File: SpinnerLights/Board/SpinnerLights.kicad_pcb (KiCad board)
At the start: 2 copper layers, 78 x 74.1 mm, 14 parts, among them U1 SeeeduinoXIAO, U2 ADXL343

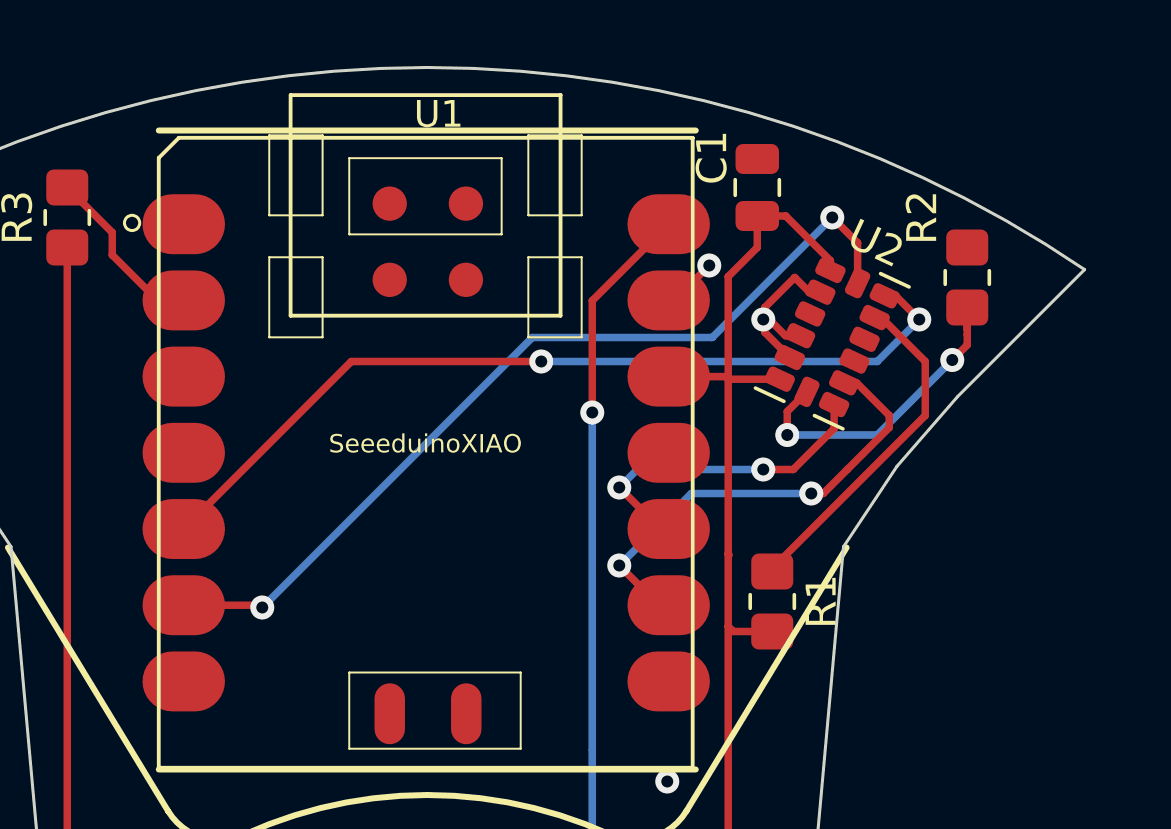
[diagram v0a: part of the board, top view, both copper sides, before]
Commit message: SpinnerLights: Fix I2C interface pins
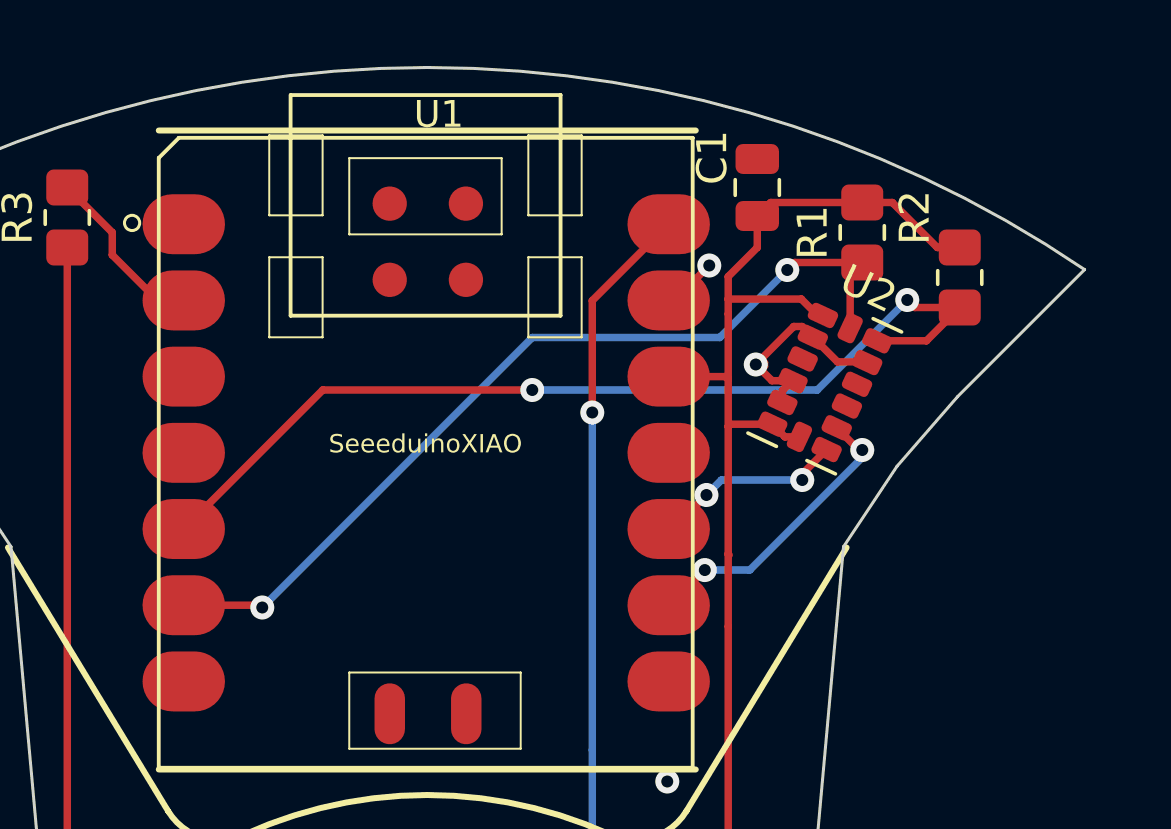
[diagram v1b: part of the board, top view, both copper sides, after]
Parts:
- moved R1 12.7 mm to (114.5, 66.5), turned to 90 degrees
- moved U2 1.52 mm to (113.2, 71.5)
- moved R2 0.25 mm to (117.8, 68.0)
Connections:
- R1 pad 1: Net-(R1-Pad1) -> SCL
- R2 pad 1: Net-(R2-Pad1) -> SDA
- R2 pad 2: GND -> +3V3
- U2 pad 12: Net-(R1-Pad1) -> GND
- U2 pad 7: Net-(R2-Pad1) -> +3V3
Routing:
- net Net-(R1-Pad1): track 11.4 -> 0.00 mm
- net Net-(R2-Pad1): track 11.0 -> 0.00 mm, vias 2 -> 0
- net +3V3: track 103.0 -> 110.1 mm
- net INT2: track 15.5 -> 10.2 mm
- net INT1: track 11.0 -> 6.74 mm
- net SDA: track 28.9 -> 32.3 mm
- net GND: track 13.3 -> 14.5 mm

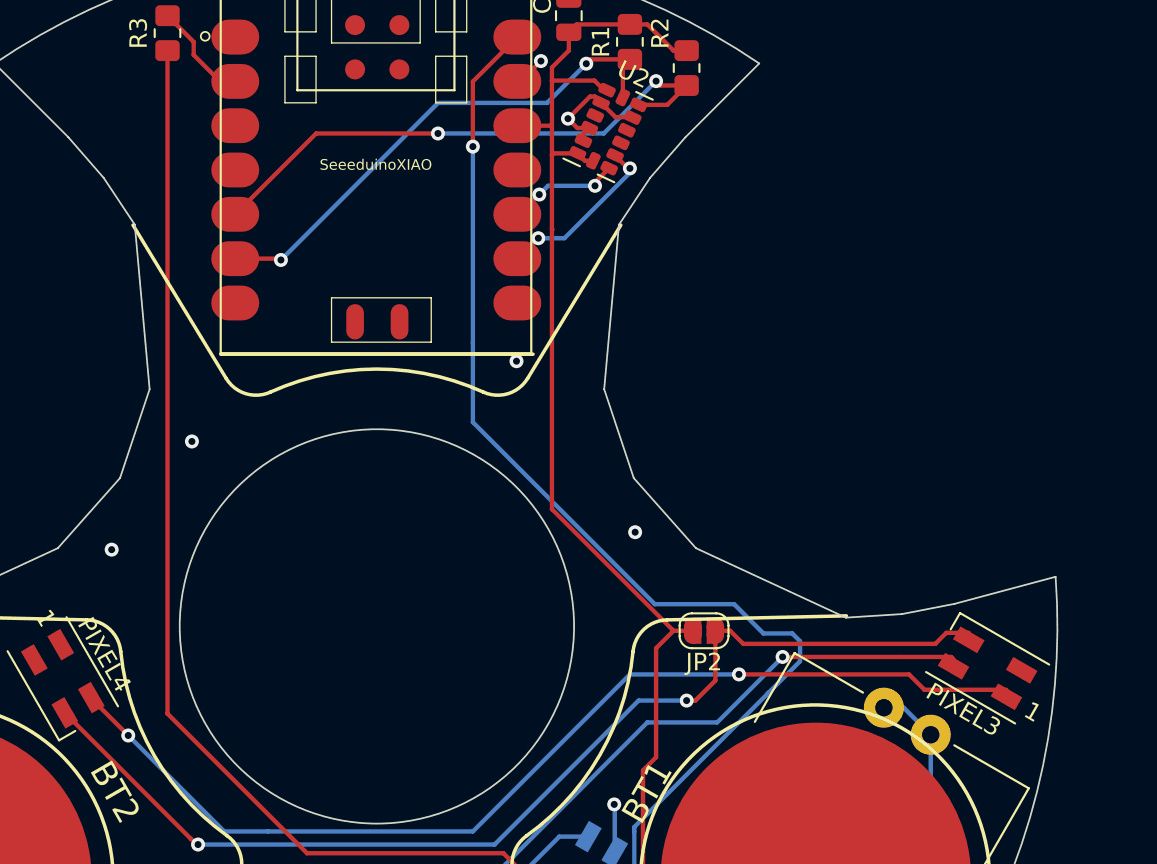
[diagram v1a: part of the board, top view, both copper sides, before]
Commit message: SpinnerLights: minor tweaks to ground plane
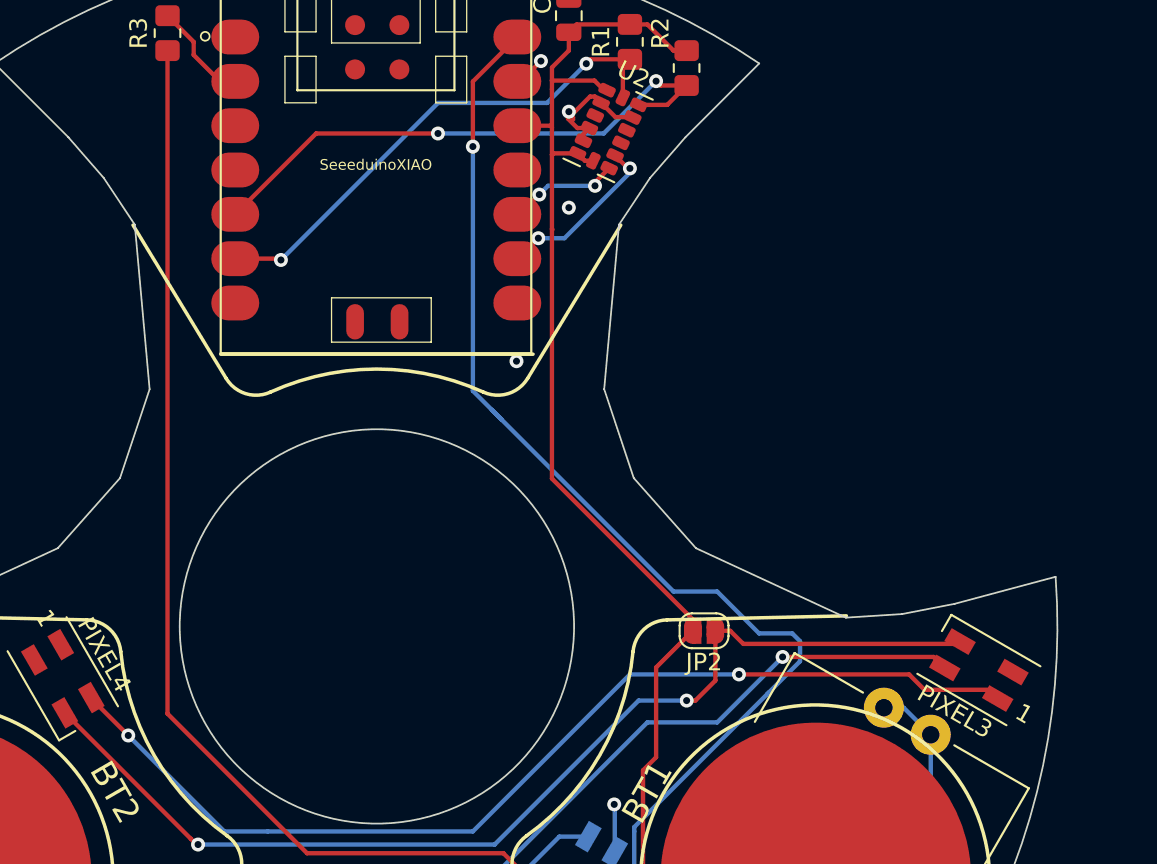
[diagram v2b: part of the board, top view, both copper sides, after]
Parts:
- moved PIXEL3 0.51 mm to (134.5, 102.5)
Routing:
- net Net-(JP2-Pad1): track 62.2 -> 61.5 mm
- net GND: vias 8 -> 6
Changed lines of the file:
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@@
     (thickness 1.6)
     (drawings 53)
-    (tracks 215)
+    (tracks 212)
     (zones 0)
     (modules 14)
@@
   )
   (module LED_SMD:LED_SK6812MINI_PLCC4_3.5x3.5mm_P1.75mm (layer F.Cu)
-    (at 135 102.4 150)
+    (at 134.5 102.5 150)
     (descr https://cdn-shop.adafruit.com/product-files/2686/SK6812MINI_REV.01-1-2.pdf)
     (tags "LED RGB NeoPixel Mini")
@@
   (segment (start 111.296956 115.953044) (end 110.5 116.75) (width 0.25) (layer B.Cu) (net 1))
   (segment (start 111.882772 115.953044) (end 111.296956 115.953044) (width 0.25) (layer B.Cu) (net 1))
-  (segment (start 117 100.25) (end 118.1 100.25) (width 0.25) (layer F.Cu) (net 1))
-  (segment (start 110.031443 93.281443) (end 117 100.25) (width 0.25) (layer F.Cu) (net 1))
   (segment (start 115.25 108.25) (end 115.25 114.5) (width 0.25) (layer F.Cu) (net 1))
   (segment (start 116 107.5) (end 115.25 108.25) (width 0.25) (layer F.Cu) (net 1))
-  (segment (start 116 101.25) (end 116 107.5) (width 0.25) (layer F.Cu) (net 1))
-  (segment (start 117 100.25) (end 116 101.25) (width 0.25) (layer F.Cu) (net 1))
   (segment (start 111.882772 116.282772) (end 112.6 117) (width 0.25) (layer B.Cu) (net 1))
   (segment (start 111.882772 115.953044) (end 111.882772 116.282772) (width 0.25) (layer B.Cu) (net 1))
   (segment (start 112.75 117) (end 115.25 114.5) (width 0.25) (layer F.Cu) (net 1))
   (segment (start 112.6 117) (end 112.75 117) (width 0.25) (layer F.Cu) (net 1))
-  (segment (start 110.031443 79.631443) (end 110.031443 93.281443) (width 0.25) (layer F.Cu) (net 1))
-  (segment (start 110.031443 77.218557) (end 110.031443 79.631443) (width 0.25) (layer F.Cu) (net 1))
   (segment (start 111.921075 73.312616) (end 111.498456 72.889997) (width 0.25) (layer F.Cu) (net 1))
   (segment (start 112.404763 73.312616) (end 111.921075 73.312616) (width 0.25) (layer F.Cu) (net 1))
@@
   (segment (start 111.45 65.5) (end 111 65.95) (width 0.25) (layer F.Cu) (net 1))
   (segment (start 114.5 65.5) (end 111.45 65.5) (width 0.25) (layer F.Cu) (net 1))
+  (segment (start 118.1 99.6) (end 118.1 100.25) (width 0.25) (layer F.Cu) (net 1))
+  (segment (start 110.031443 91.531443) (end 118.1 99.6) (width 0.25) (layer F.Cu) (net 1))
+  (segment (start 110.031443 77.218557) (end 110.031443 91.531443) (width 0.25) (layer F.Cu) (net 1))
+  (segment (start 116 102.35) (end 118.1 100.25) (width 0.25) (layer F.Cu) (net 1))
+  (segment (start 116 107.5) (end 116 102.35) (width 0.25) (layer F.Cu) (net 1))
   (segment (start 108.047195 68.764277) (end 106.835723 68.764277) (width 0.25) (layer F.Cu) (net 2))
   (via (at 79 127.6) (size 0.8) (drill 0.4) (layers F.Cu B.Cu) (net 2))
@@
   (segment (start 108.235723 68.764277) (end 109.4 67.6) (width 0.25) (layer F.Cu) (net 2))
   (segment (start 108.047195 68.764277) (end 108.235723 68.764277) (width 0.25) (layer F.Cu) (net 2))
-  (via (at 110.95 70.9) (size 0.8) (drill 0.4) (layers F.Cu B.Cu) (net 2))
   (via (at 108 84.8) (size 0.8) (drill 0.4) (layers F.Cu B.Cu) (net 2))
-  (via (at 114.8 94.6) (size 0.8) (drill 0.4) (layers F.Cu B.Cu) (net 2))
-  (via (at 89.4 89.4) (size 0.8) (drill 0.4) (layers F.Cu B.Cu) (net 2))
-  (via (at 84.8 95.6) (size 0.8) (drill 0.4) (layers F.Cu B.Cu) (net 2))
   (segment (start 113.672953 70.811931) (end 112.850834 69.989812) (width 0.25) (layer F.Cu) (net 2))
   (segment (start 114.640332 70.811931) (end 113.672953 70.811931) (width 0.25) (layer F.Cu) (net 2))
@@
   (segment (start 111.489905 71.439905) (end 110.95 70.9) (width 0.25) (layer F.Cu) (net 2))
   (segment (start 112.174645 71.439905) (end 111.489905 71.439905) (width 0.25) (layer F.Cu) (net 2))
+  (via (at 111 70.5) (size 0.8) (drill 0.4) (layers F.Cu B.Cu) (net 2))
+  (via (at 111 76) (size 0.8) (drill 0.4) (layers F.Cu B.Cu) (net 2))
   (segment (start 116.590673 126.725) (end 116.475 126.725) (width 0.25) (layer F.Cu) (net 3))
   (segment (start 114.75 125) (end 114.75 123.75) (width 0.25) (layer F.Cu) (net 3))
@@
   (segment (start 105.5 68.771472) (end 108.047195 66.224277) (width 0.25) (layer F.Cu) (net 3))
   (segment (start 105.5 72.5) (end 105.5 68.771472) (width 0.25) (layer F.Cu) (net 3))
-  (segment (start 105.5 83.75) (end 105.5 72.5) (width 0.25) (layer B.Cu) (net 3))
-  (segment (start 115.925 98.725) (end 105.5 88.3) (width 0.25) (layer B.Cu) (net 3))
-  (segment (start 120.475 98.725) (end 115.925 98.725) (width 0.25) (layer B.Cu) (net 3))
-  (segment (start 105.5 88.3) (end 105.5 83.75) (width 0.25) (layer B.Cu) (net 3))
-  (segment (start 122.15 100.4) (end 120.475 98.725) (width 0.25) (layer B.Cu) (net 3))
-  (segment (start 123.8 100.4) (end 122.15 100.4) (width 0.25) (layer B.Cu) (net 3))
+  (segment (start 119.5 98) (end 117 98) (width 0.25) (layer B.Cu) (net 3))
+  (segment (start 121.9 100.4) (end 119.5 98) (width 0.25) (layer B.Cu) (net 3))
+  (segment (start 123.8 100.4) (end 121.9 100.4) (width 0.25) (layer B.Cu) (net 3))
   (segment (start 124.25 100.85) (end 123.8 100.4) (width 0.25) (layer B.Cu) (net 3))
   (segment (start 124.25 102) (end 124.25 100.85) (width 0.25) (layer B.Cu) (net 3))
   (segment (start 122.375 103.875) (end 124.25 102) (width 0.25) (layer B.Cu) (net 3))
+  (segment (start 105.5 72.5) (end 105.5 86.5) (width 0.25) (layer B.Cu) (net 3))
+  (segment (start 105.5 86.5) (end 107.125 88.125) (width 0.25) (layer B.Cu) (net 3))
+  (segment (start 107.125 88.125) (end 106.575 87.575) (width 0.25) (layer B.Cu) (net 3))
+  (segment (start 117 98) (end 107.125 88.125) (width 0.25) (layer B.Cu) (net 3))
   (via (at 117.75 104.25) (size 0.8) (drill 0.4) (layers F.Cu B.Cu) (net 4))
   (segment (start 115 104.25) (end 117.75 104.25) (width 0.25) (layer B.Cu) (net 4))
@@
   (segment (start 89.75 112.5) (end 89.664184 112.5) (width 0.25) (layer F.Cu) (net 4))
   (segment (start 82.117228 104.953044) (end 89.332092 112.167908) (width 0.25) (layer F.Cu) (net 4))
-  (segment (start 119.4 100.25) (end 120.25 100.25) (width 0.25) (layer F.Cu) (net 4))
+  (segment (start 133.289184 101) (end 133.421956 100.867228) (width 0.25) (layer F.Cu) (net 4))
+  (segment (start 121 101) (end 133.289184 101) (width 0.25) (layer F.Cu) (net 4))
   (segment (start 120.25 100.25) (end 121 101) (width 0.25) (layer F.Cu) (net 4))
-  (segment (start 121 101) (end 132 101) (width 0.25) (layer F.Cu) (net 4))
-  (segment (start 132.632772 100.367228) (end 133.921956 100.367228) (width 0.25) (layer F.Cu) (net 4))
-  (segment (start 132 101) (end 132.632772 100.367228) (width 0.25) (layer F.Cu) (net 4))
+  (segment (start 119.4 100.25) (end 120.25 100.25) (width 0.25) (layer F.Cu) (net 4))
   (via (at 109 114.75) (size 0.8) (drill 0.4) (layers F.Cu B.Cu) (net 5))
   (segment (start 109.328044 115.078044) (end 109 114.75) (width 0.25) (layer B.Cu) (net 5))
@@
   (segment (start 81.132772 128.882772) (end 82.953044 128.882772) (width 0.25) (layer B.Cu) (net 6))
   (segment (start 80.75 128.5) (end 81.132772 128.882772) (width 0.25) (layer B.Cu) (net 6))
-  (segment (start 132.914184 101.75) (end 133.046956 101.882772) (width 0.25) (layer F.Cu) (net 7))
-  (segment (start 130 101.75) (end 132.914184 101.75) (width 0.25) (layer F.Cu) (net 7))
   (segment (start 119.5 105.5) (end 115.5 105.5) (width 0.25) (layer B.Cu) (net 7))
   (segment (start 123.25 101.75) (end 119.5 105.5) (width 0.25) (layer B.Cu) (net 7))
@@
   (segment (start 106 115) (end 92.25 115) (width 0.25) (layer B.Cu) (net 7))
   (via (at 123.25 101.75) (size 0.8) (drill 0.4) (layers F.Cu B.Cu) (net 7))
-  (segment (start 130 101.75) (end 123.25 101.75) (width 0.25) (layer F.Cu) (net 7))
-  (segment (start 136.078044 103.632772) (end 131.382772 103.632772) (width 0.25) (layer F.Cu) (net 8))
+  (segment (start 131.914184 101.75) (end 132.546956 102.382772) (width 0.25) (layer F.Cu) (net 7))
+  (segment (start 123.25 101.75) (end 131.914184 101.75) (width 0.25) (layer F.Cu) (net 7))
   (segment (start 131.382772 103.632772) (end 130.5 102.75) (width 0.25) (layer F.Cu) (net 8))
   (via (at 120.75 102.75) (size 0.8) (drill 0.4) (layers F.Cu B.Cu) (net 8))
@@
   (segment (start 83.632772 104.132772) (end 83.632772 104.078044) (width 0.25) (layer F.Cu) (net 8))
   (segment (start 85.75 106.25) (end 83.632772 104.132772) (width 0.25) (layer F.Cu) (net 8))
+  (segment (start 135.078044 103.632772) (end 135.578044 104.132772) (width 0.25) (layer F.Cu) (net 8))
+  (segment (start 131.382772 103.632772) (end 135.078044 103.632772) (width 0.25) (layer F.Cu) (net 8))
   (segment (start 91.882635 68.764277) (end 91.014277 68.764277) (width 0.25) (layer F.Cu) (net 10))
   (segment (start 91.014277 68.764277) (end 89.5 67.25) (width 0.25) (layer F.Cu) (net 10))

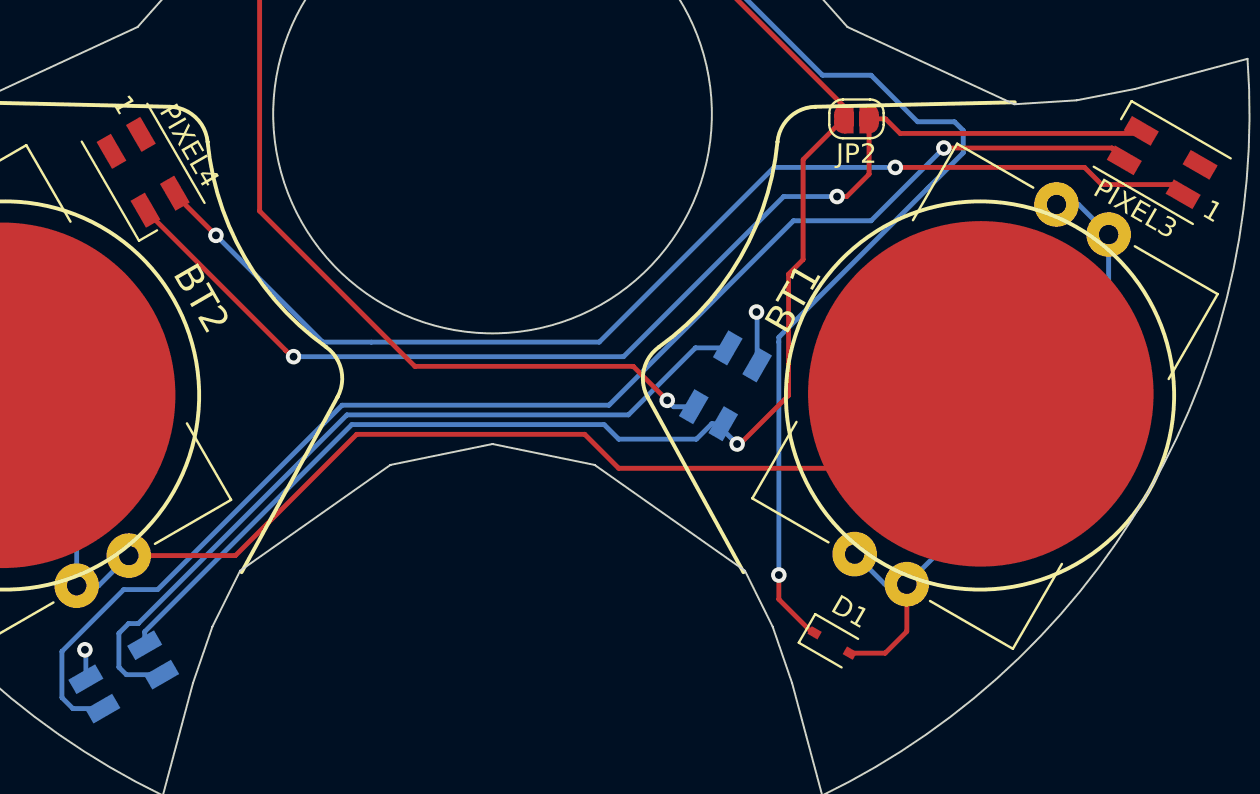
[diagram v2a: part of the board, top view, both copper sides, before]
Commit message: SpinnerLights: Fix symbols for NeoPixels
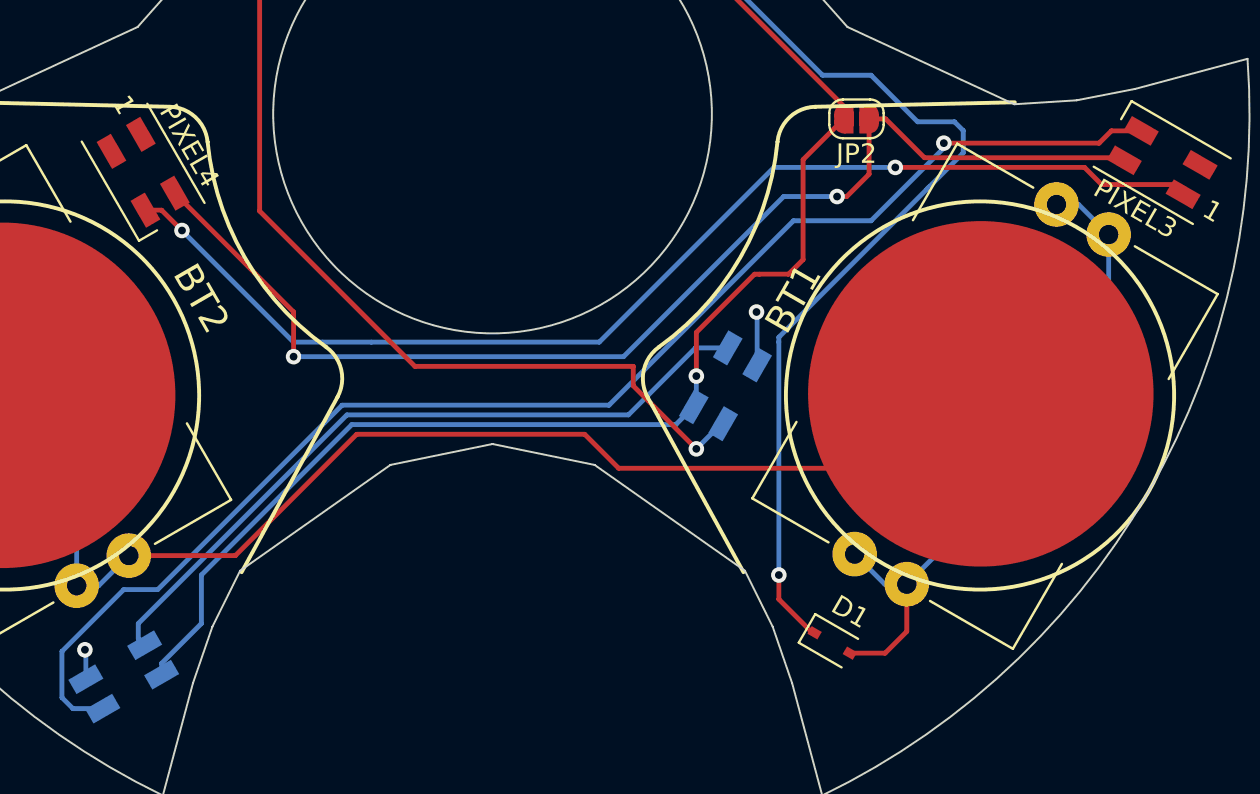
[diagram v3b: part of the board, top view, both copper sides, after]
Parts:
- PIXEL2, PIXEL3, PIXEL4, Pixel1: value NeoPixel_THT -> SK6812MINI
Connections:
- net Net-(BT1-PadN) renamed /B15
- PIXEL2 pad 3: +3V3 -> Net-(PIXEL2-Pad3)
- PIXEL2 pad 4: Net-(PIXEL2-Pad4) -> +3V3
- PIXEL3 pad 3: Net-(JP2-Pad1) -> Net-(PIXEL2-Pad1)
- PIXEL3 pad 4: Net-(PIXEL2-Pad1) -> Net-(JP2-Pad1)
- PIXEL4 pad 3: Net-(JP2-Pad1) -> Net-(PIXEL3-Pad1)
- PIXEL4 pad 4: Net-(PIXEL3-Pad1) -> Net-(JP2-Pad1)
- Pixel1 pad 1: Net-(PIXEL2-Pad4) -> Net-(PIXEL2-Pad3)
- Pixel1 pad 3: +3V3 -> Net-(Pixel1-Pad3)
- Pixel1 pad 4: Net-(Pixel1-Pad4) -> +3V3
- R3 pad 1: Net-(Pixel1-Pad4) -> Net-(Pixel1-Pad3)
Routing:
- net Net-(Pixel1-Pad3): track 0.00 -> 68.5 mm, vias 0 -> 1
- net Net-(Pixel1-Pad4): track 64.5 -> 0.00 mm, vias 1 -> 0
- net Net-(PIXEL2-Pad4): track 41.6 -> 0.00 mm
- net Net-(PIXEL2-Pad3): track 0.00 -> 37.5 mm
- net +3V3: track 109.9 -> 107.8 mm
- net Net-(PIXEL2-Pad1): track 70.5 -> 71.8 mm
- net Net-(PIXEL3-Pad1): track 59.5 -> 60.6 mm
